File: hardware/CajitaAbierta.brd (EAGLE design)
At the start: 32.1 x 61.8 mm, 30 parts

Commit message: Last minute changes to version 0.3
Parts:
- moved R1 0.63 mm to (22.4, 24.1)
- moved R2 0.63 mm to (22.5, 21.0)
- moved R3 0.63 mm to (22.5, 18.0)
- moved R4 0.63 mm to (22.5, 15.0)
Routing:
- net ADC5: track 31.0 -> 32.9 mm
- net ADC6: track 25.3 -> 26.8 mm
- net ADC4: track 27.4 -> 28.7 mm
- net ADC7: track 31.8 -> 33.1 mm
- net 3V3: track 62.9 -> 63.6 mm
- net SPI_CLK: track 38.5 -> 39.1 mm

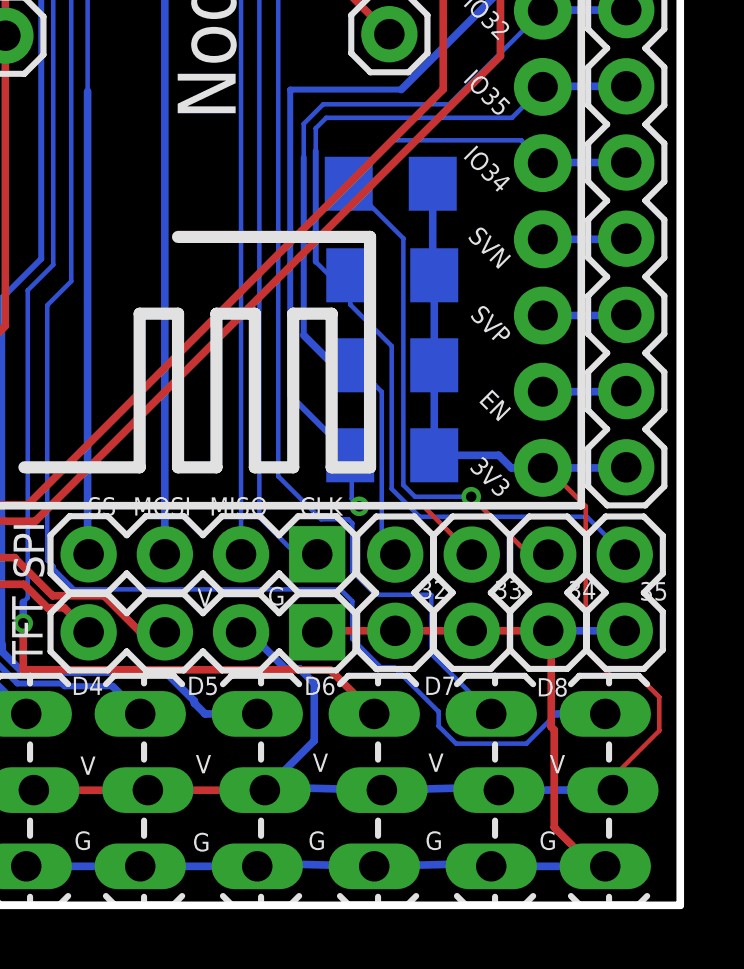
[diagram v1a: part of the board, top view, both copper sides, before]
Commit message: Voltage divider uses V+ as variable resistance
For Yesi :)
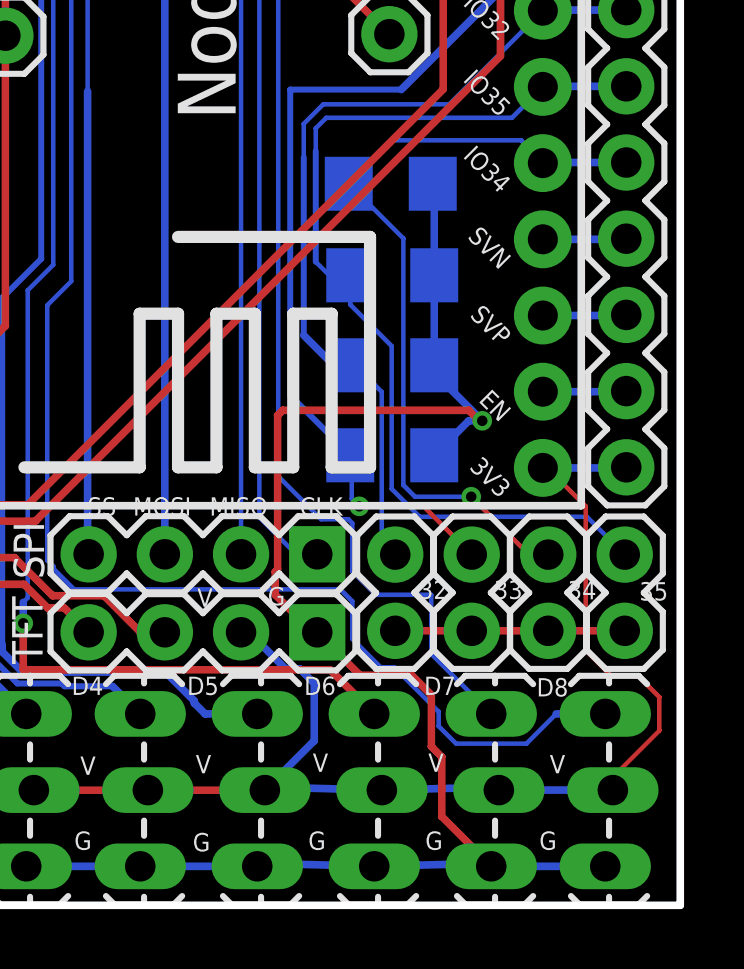
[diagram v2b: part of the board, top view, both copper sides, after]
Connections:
- net 3V3: now also 32.1, 33.1, 34.1, 35.1; no longer R1.1, R2.1, R3.1, R4.1
- net GND: now also R1.1, R2.1, R3.1, R4.1; no longer 32.1, 33.1, 34.1, 35.1
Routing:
- net GND: track 153.3 -> 171.1 mm, vias 0 -> 1
- net 3V3: track 63.6 -> 58.5 mm
